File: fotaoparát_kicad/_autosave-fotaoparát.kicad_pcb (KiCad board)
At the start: 4 copper layers, 34 parts, among them J1 Conn_01x01_Pin, J10 Conn_01x01_Pin, J11 Conn_01x01_Pin, J12 Conn_01x01_Pin, J2 Conn_01x01_Pin, J3 Conn_01x01_Pin, J4 Conn_01x01_Pin, J5 Conn_01x01_Pin, J6 Conn_01x01_Pin, J7 Conn_01x01_Pin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

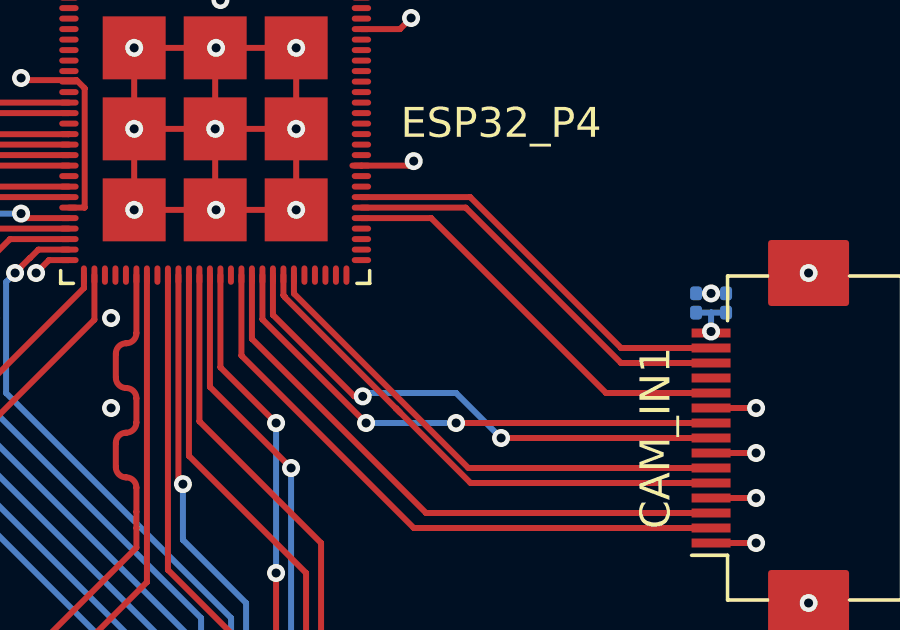
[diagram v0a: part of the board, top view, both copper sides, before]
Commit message: delal jsem pullups
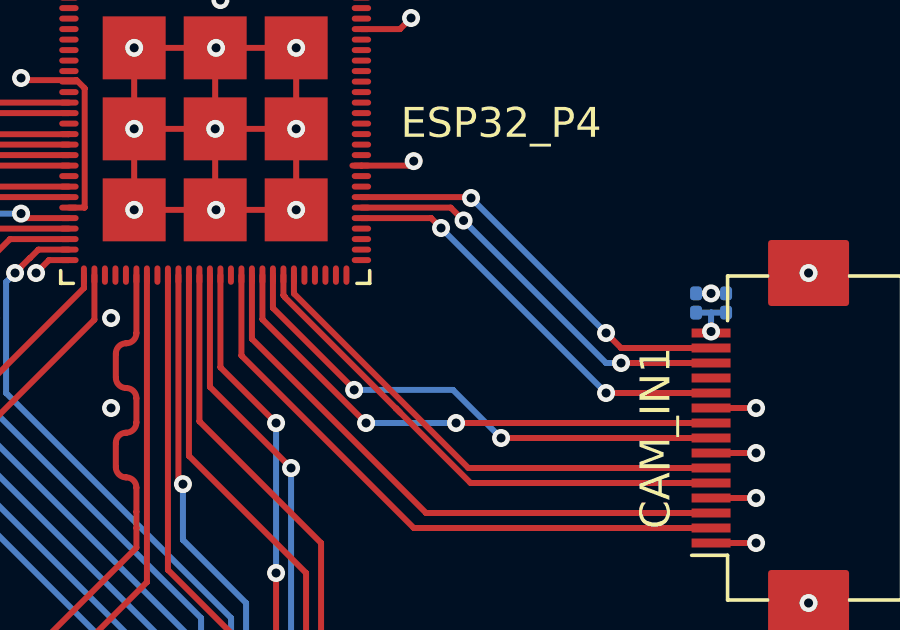
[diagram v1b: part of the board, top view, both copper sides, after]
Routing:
- net Net-(CAM_IN1-Pin_14): vias 0 -> 2
- net Net-(CAM_IN1-Pin_11): vias 0 -> 2
- net Net-(CAM_IN1-Pin_13): vias 0 -> 2
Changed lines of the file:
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@@
 	)
 	(segment
-		(start 170 91)
-		(end 164.97 85.97)
+		(start 169.5 90.5)
+		(end 170 91)
 		(width 0.2)
 		(layer "F.Cu")
@@
 	)
 	(segment
-		(start 169.5 92.5)
-		(end 163.67 86.67)
-		(width 0.2)
-		(layer "F.Cu")
-		(net 4)
+		(start 164.97 85.97)
+		(end 165 86)
+		(width 0.2)
+		(layer "F.Cu")
+		(net 3)
+	)
+	(via
+		(at 165 86)
+		(size 0.6)
+		(drill 0.3)
+		(layers "F.Cu" "B.Cu")
+		(net 3)
+	)
+	(via
+		(at 169.5 90.5)
+		(size 0.6)
+		(drill 0.3)
+		(layers "F.Cu" "B.Cu")
+		(net 3)
+	)
+	(segment
+		(start 165 86)
+		(end 169.5 90.5)
+		(width 0.2)
+		(layer "B.Cu")
+		(net 3)
 	)
 	(segment
@@
 	)
 	(segment
+		(start 163.67 86.67)
+		(end 164 87)
+		(width 0.2)
+		(layer "F.Cu")
+		(net 4)
+	)
+	(segment
 		(start 173 92.5)
 		(end 169.5 92.5)
@@
 		(net 4)
 	)
+	(via
+		(at 164 87)
+		(size 0.6)
+		(drill 0.3)
+		(layers "F.Cu" "B.Cu")
+		(net 4)
+	)
+	(via
+		(at 169.5 92.5)
+		(size 0.6)
+		(drill 0.3)
+		(layers "F.Cu" "B.Cu")
+		(net 4)
+	)
+	(segment
+		(start 164 87)
+		(end 169.5 92.5)
+		(width 0.2)
+		(layer "B.Cu")
+		(net 4)
+	)
 	(segment
 		(start 148.001355 85.62)
@@
 	)
 	(segment
-		(start 170 91.5)
-		(end 164.82 86.32)
+		(start 164.32 86.32)
+		(end 161.345 86.32)
 		(width 0.2)
 		(layer "F.Cu")
@@
 	)
 	(segment
-		(start 164.82 86.32)
-		(end 161.345 86.32)
-		(width 0.2)
-		(layer "F.Cu")
+		(start 164.75 86.75)
+		(end 164.32 86.32)
+		(width 0.2)
+		(layer "F.Cu")
+		(net 7)
+	)
+	(via
+		(at 170 91.5)
+		(size 0.6)
+		(drill 0.3)
+		(layers "F.Cu" "B.Cu")
+		(net 7)
+	)
+	(via
+		(at 164.75 86.75)
+		(size 0.6)
+		(drill 0.3)
+		(layers "F.Cu" "B.Cu")
+		(net 7)
+	)
+	(segment
+		(start 169.5 91.5)
+		(end 170 91.5)
+		(width 0.2)
+		(layer "B.Cu")
+		(net 7)
+	)
+	(segment
+		(start 164.75 86.75)
+		(end 169.5 91.5)
+		(width 0.2)
+		(layer "B.Cu")
 		(net 7)
 	)
@@
 	)
 	(segment
-		(start 161.388156 92.611844)
-		(end 161.111844 92.611844)
+		(start 161.111844 92.388156)
+		(end 161.103554 92.396446)
 		(width 0.2)
 		(layer "F.Cu")
@@
 	)
 	(segment
-		(start 161.111844 92.611844)
-		(end 158.395 89.895)
-		(width 0.2)
-		(layer "F.Cu")
-		(net 71)
-	)
-	(segment
-		(start 158.395 89.895)
-		(end 158.395 88.57)
+		(start 161.111844 92.383179)
+		(end 161.111844 92.388156)
 		(width 0.2)
 		(layer "F.Cu")
@@
 		(net 71)
 	)
-	(via
-		(at 161.388156 92.611844)
-		(size 0.6)
-		(drill 0.3)
-		(layers "F.Cu" "B.Cu")
+	(segment
+		(start 158.395 89.666335)
+		(end 158.395 88.57)
+		(width 0.2)
+		(layer "F.Cu")
 		(net 71)
 	)
+	(segment
+		(start 161.111844 92.383179)
+		(end 158.395 89.666335)
+		(width 0.2)
+		(layer "F.Cu")
+		(net 71)
+	)
 	(via
 		(at 166 94)
@@
 		(net 71)
 	)
-	(segment
-		(start 161.5 92.5)
-		(end 164.5 92.5)
-		(width 0.2)
-		(layer "B.Cu")
+	(via
+		(at 161.103554 92.396446)
+		(size 0.6)
+		(drill 0.3)
+		(layers "F.Cu" "B.Cu")
 		(net 71)
 	)
 	(segment
-		(start 164.5 92.5)
+		(start 164.396446 92.396446)
 		(end 166 94)
 		(width 0.2)
@@
 	)
 	(segment
-		(start 161.388156 92.611844)
-		(end 161.5 92.5)
-		(width 0.2)
-		(layer "B.Cu")
+		(start 161.103554 92.396446)
+		(end 164.396446 92.396446)
+		(width 0.2)
+		(layer "B.Cu")
